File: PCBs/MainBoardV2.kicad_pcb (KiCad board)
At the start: 2 copper layers, 40.4 x 70 mm, 38 parts, among them IC1 PASCO2V01BUMA1, J1 Conn_01x12_FPC_0.5mm, J4 SM06B-GHS-TB, J5 USB_C_Receptacle, SW1 SMD_4.6x2.8mm_h2.5mm, SW2 SMD_4.6x2.8mm_h2.5mm, SW3 PTH_RA_h7.5mm, U1 AP3012, U2 ESP32-S3-WROOM-1-N16R2, U5 AP2112K-3.3

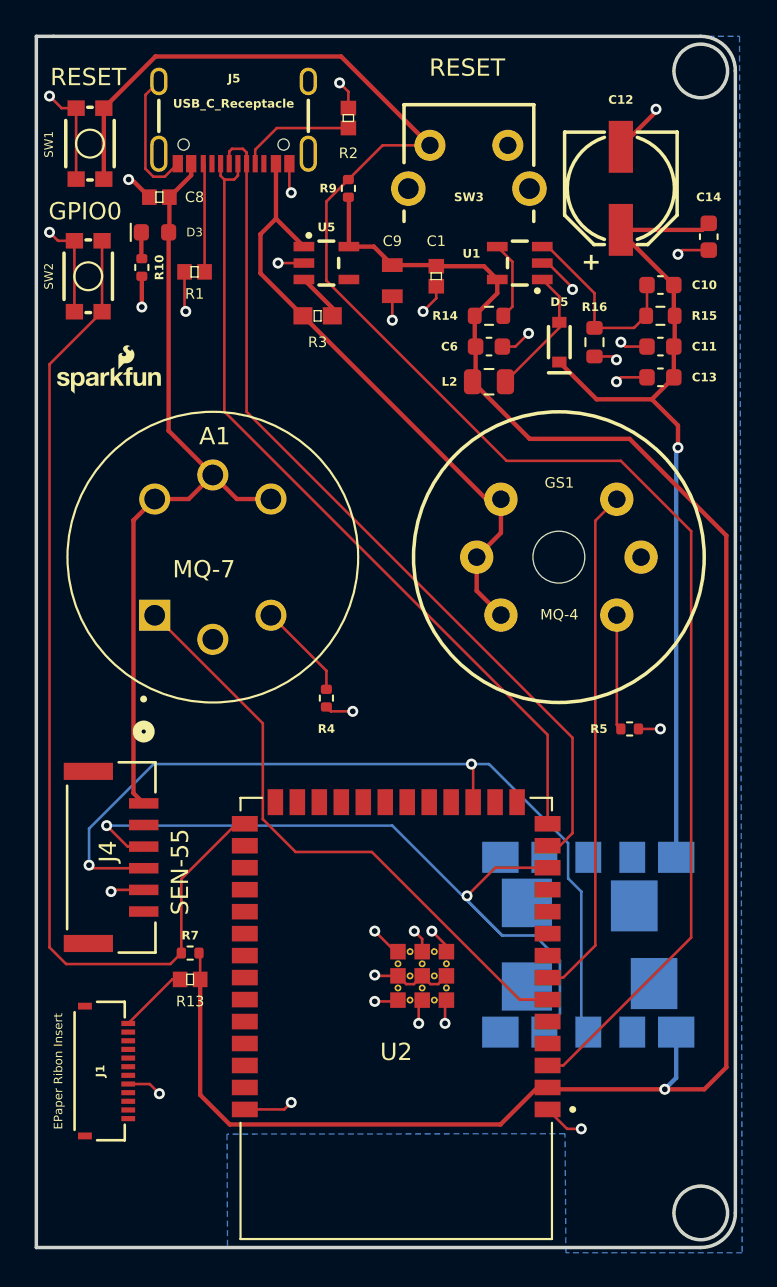
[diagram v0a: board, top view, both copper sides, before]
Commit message: Ready for Air Review
Main Board PCB FILES ready for Schematic and Air Wire Review
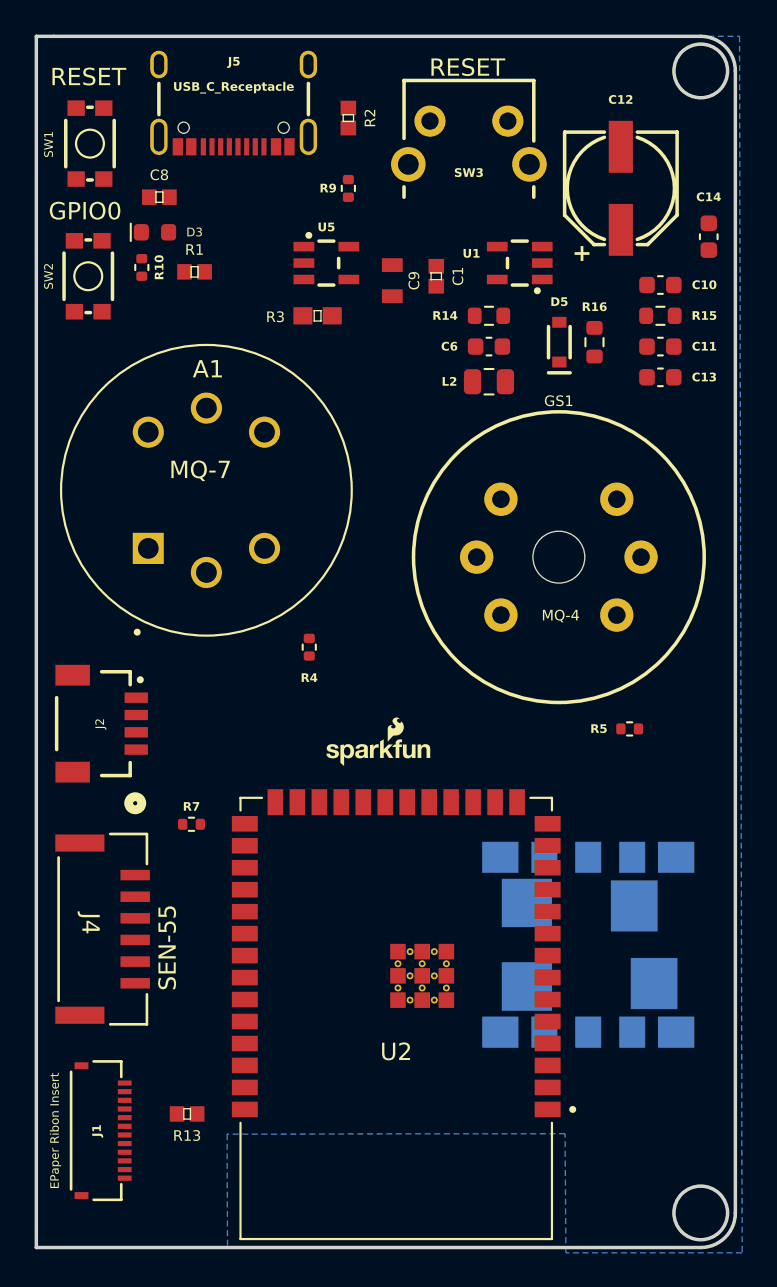
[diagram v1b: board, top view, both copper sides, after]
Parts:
- added J2: Qwiic_RA, SparkFun-Connector:JST04_1MM_RA, F.Cu at (134.6, 93.6)
- moved G*** 26.6 mm to (148.5, 95.2)
- moved R13 7.77 mm to (137.5, 116.2)
- moved R7 7.44 mm to (137.8, 99.4)
- moved J4 4.17 mm to (132.6, 105.5)
- moved A1 3.88 mm to (138.6, 80.1)
- moved J1 3.45 mm to (132.6, 117.1)
- moved R4 3.11 mm to (144.6, 89.2)
- moved SW3 1.40 mm to (153.8, 58.8)
- moved J5 0.98 mm to (140.2, 60.6)
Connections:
- C12 pad +: /12V -> (no net)
- C12 pad -: GND -> (no net)
- U2 pad 10: /LEDPWM -> unconnected-(U2-IO17-Pad10)
- U2 pad 16: /BUSY_N -> unconnected-(U2-IO46-Pad16)
- U2 pad 18: /D/C -> unconnected-(U2-IO10-Pad18)
- U2 pad 28: unconnected-(U2-IO35-Pad28) -> /BUSY_N(GPIO)
- U2 pad 29: unconnected-(U2-IO36-Pad29) -> /SCL-Epaper(SPI)
- U2 pad 30: unconnected-(U2-IO37-Pad30) -> /SDA-Epaper(SPI)
- U2 pad 31: unconnected-(U2-IO38-Pad31) -> /CSB(SPI)
- U2 pad 32: unconnected-(U2-IO39-Pad32) -> /D/C(GPIO)
- U2 pad 33: unconnected-(U2-IO40-Pad33) -> /RST_N(GPIO)
- U2 pad 34: /CSB -> unconnected-(U2-IO41-Pad34)
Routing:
- net /3.3VOUT: track 112.2 -> 0.00 mm, vias 1 -> 0
- net /RESET: track 100.1 -> 0.00 mm
- net /5V-IN: track 82.0 -> 0.00 mm
- net GND: track 73.1 -> 0.00 mm, vias 30 -> 0
- net /ESP_0: track 59.7 -> 0.00 mm
- net /D-: track 50.7 -> 0.00 mm
- net /12V: track 50.2 -> 0.00 mm, vias 1 -> 0
- net /SCL: track 50.1 -> 0.00 mm, vias 2 -> 0
- net /D+: track 47.6 -> 0.00 mm
- net /SDA: track 45.0 -> 0.00 mm, vias 2 -> 0
- net /MQ7-DATA: track 35.2 -> 0.00 mm
- net /MQ4-DATA: track 29.8 -> 0.00 mm
- net Net-(U1-FB): track 11.2 -> 0.00 mm
- net Net-(U1-SW): track 7.61 -> 0.00 mm
- net Net-(J5-CC1): track 6.71 -> 0.00 mm
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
